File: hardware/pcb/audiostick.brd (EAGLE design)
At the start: 83 x 40 mm, 65 parts, among them IC1 TPS73633MBDV, IC3 PCM5102ASW, IC5 AP22804W5, IC6 TINY13V-10SSU, J1 AVRISP6TH127, J2 AUDIO_JACK_3.5MM_PTH, J3 USB-B

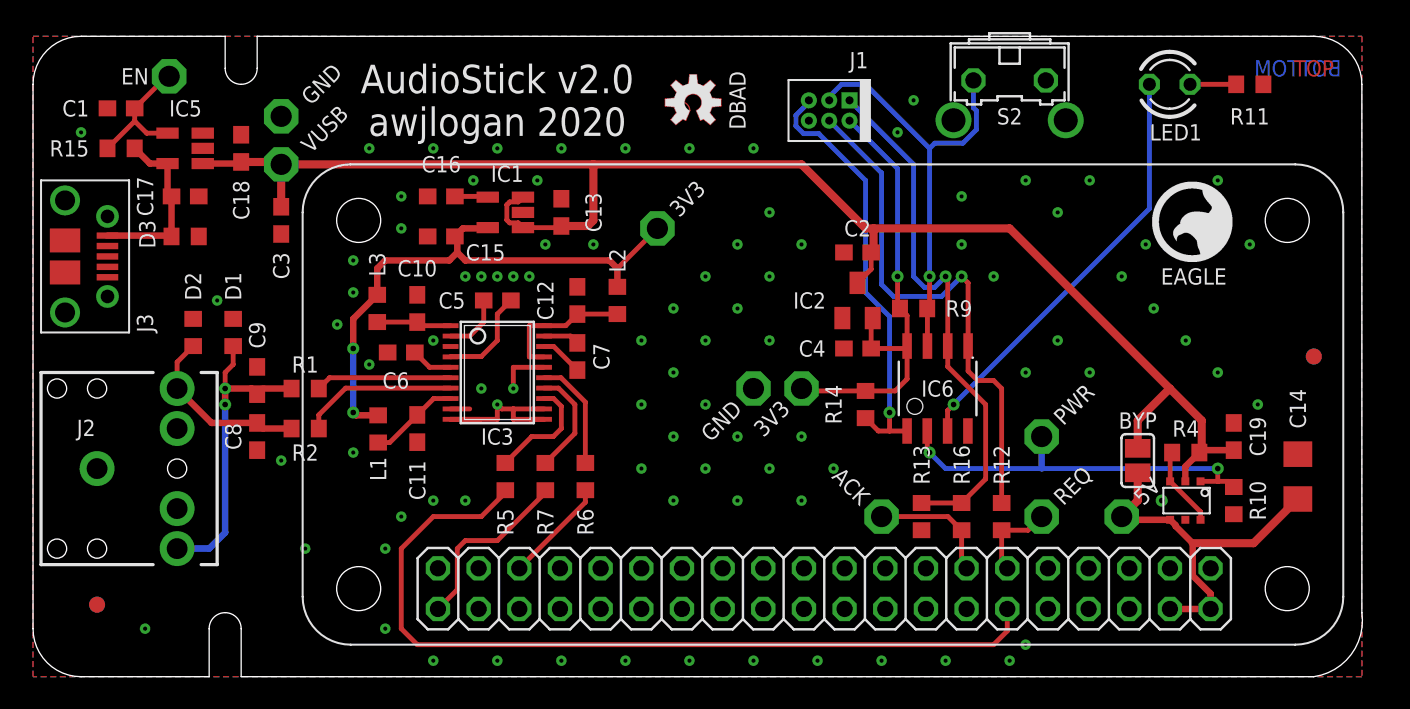
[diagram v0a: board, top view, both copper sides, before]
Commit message: Complete revision of design - layout, connections, parts. Ready for proto run
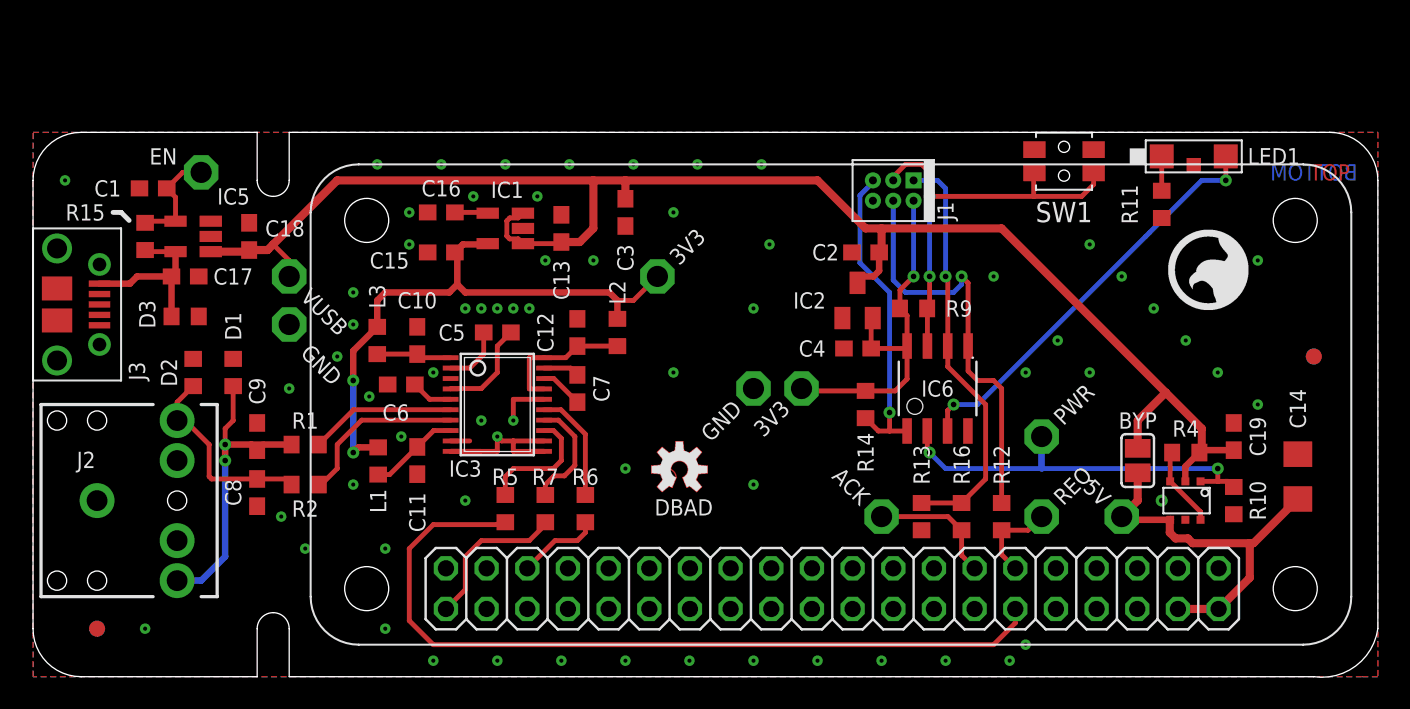
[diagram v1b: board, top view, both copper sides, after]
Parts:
- removed S2: (no value), switch-omron:B3F-31XX
- added SW1: EVQP7, AudioStick:EVQP7L
- LED1: value (none) -> LEDLED; device led:LED3MM -> AudioStick:KPA-3010
- moved C3 21.5 mm to (37.0, 29.0)
- moved TP8 13.0 mm to (16.0, 22.0)
- moved R11 9.30 mm to (70.5, 29.5), turned to 90 degrees
- moved TP4 7.02 mm to (16.0, 25.0)
- moved J1 6.40 mm to (55.0, 31.0)
- moved TP10 6.32 mm to (10.5, 31.5)
- moved R15 5.70 mm to (7.00, 27.5), turned to 270 degrees
- moved C18 5.52 mm to (13.5, 27.5)
- moved IC5 5.52 mm to (10.0, 27.5)
- moved C1 5.39 mm to (7.50, 30.5)
- moved C17 5.00 mm to (9.50, 25.0)
- moved D3 5.00 mm to (9.50, 22.5)
- moved LED1 4.74 mm to (72.5, 32.5)
- moved C8 3.50 mm to (14.0, 11.5)
- moved C9 3.50 mm to (14.0, 15.0)
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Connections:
- net GND: now also SW1.2A, SW1.2B; no longer S2.1
- net N$15: now also LED1.C; no longer LED1.K
- net SW: now also SW1.1A, SW1.1B; no longer S2.2
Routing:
- net ACK: track 33.5 -> 26.0 mm
- net !RST: track 26.9 -> 19.7 mm
- net REQ: track 33.2 -> 26.0 mm
- net +3V3: track 29.1 -> 22.9 mm
- net BCK: track 53.1 -> 51.1 mm
- net IN_EN: track 8.54 -> 6.78 mm
- net DIN: track 11.4 -> 9.75 mm
- net +5V: track 97.8 -> 99.4 mm
- net LRCK: track 6.59 -> 5.20 mm
- net VOR: track 11.2 -> 12.5 mm
- net VCCINT: track 35.1 -> 36.3 mm
- net N$8: track 9.78 -> 10.8 mm
- net SW: track 27.6 -> 26.7 mm, vias 1 -> 2
- net +5V/1: track 23.1 -> 23.9 mm
- net VOL: track 19.7 -> 18.9 mm
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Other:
- board size 83 x 40 mm -> 84 x 34 mm
- board text removed: "EAGLE"
